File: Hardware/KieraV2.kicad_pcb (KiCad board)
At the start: 2 copper layers, 111 x 63.2 mm, 87 parts, among them J1 Conn_01x04_Male, J2 Conn_01x05_Male, SW1 SW_Rotary2x4, SW2 SW_Rotary2x4, SW3 SW_Push, SW4 SW_Push, SW5 SW_Push, SW6 SW_Push, SW7 SW_MEC_5G, U1 STM32L4P5RET6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

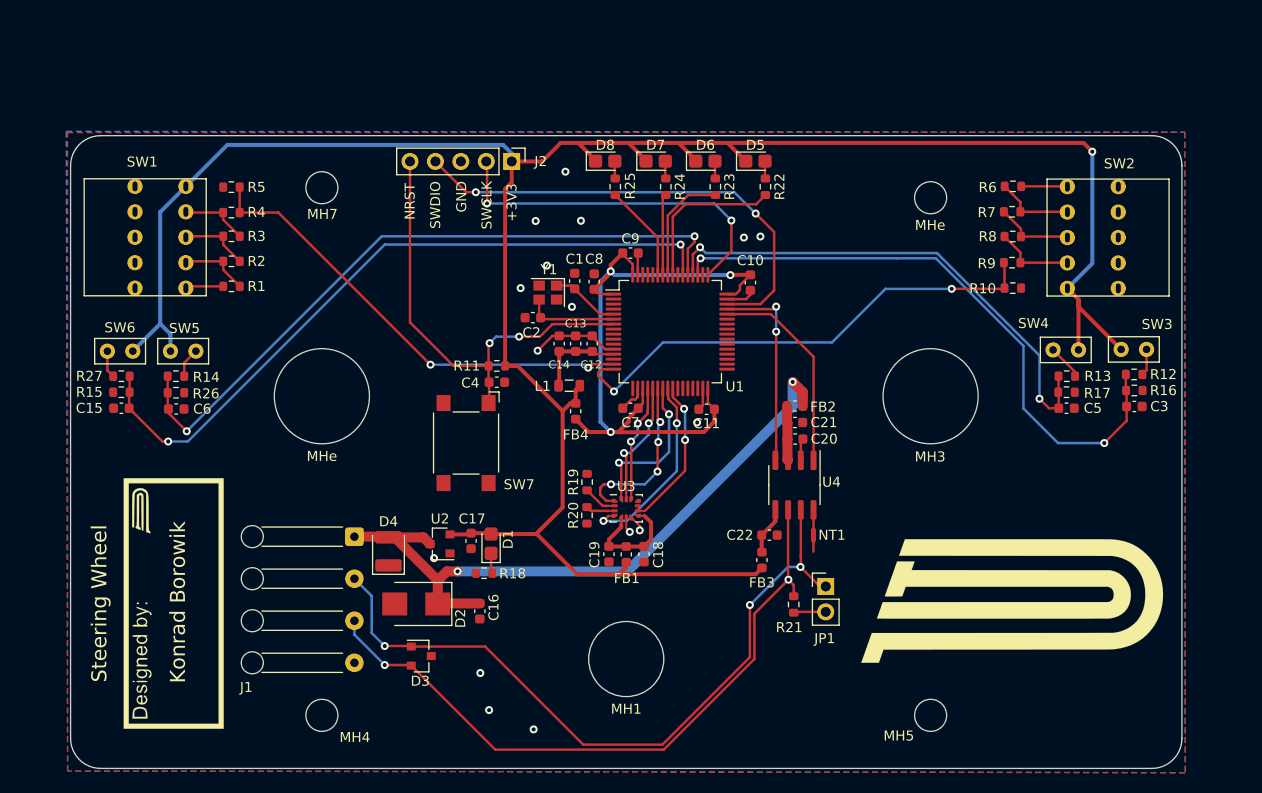
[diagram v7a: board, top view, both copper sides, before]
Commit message: changed imu footprint
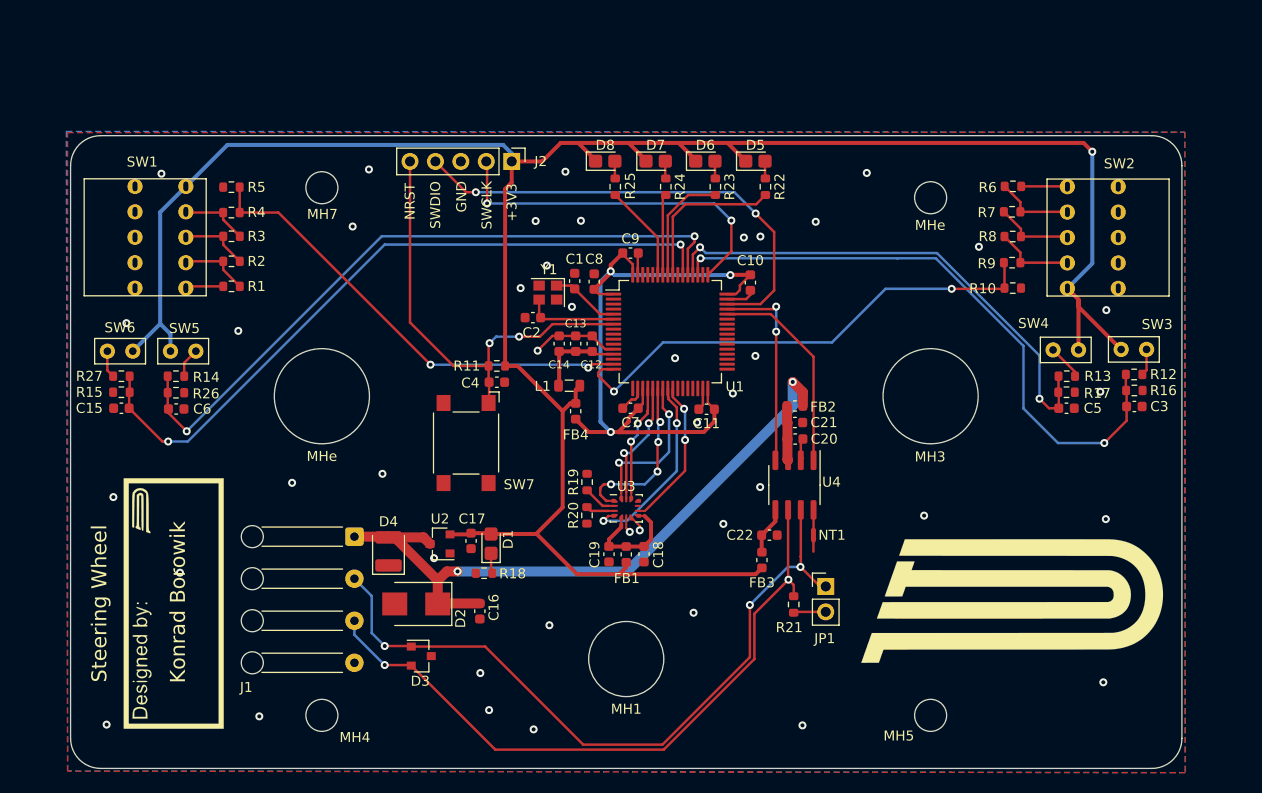
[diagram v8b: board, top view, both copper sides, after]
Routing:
- net GND: vias 16 -> 45
